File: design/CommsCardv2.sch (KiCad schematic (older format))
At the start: 0 parts

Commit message: Remove annotation
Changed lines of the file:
@@
 $EndSheet
 $Sheet
-S 2050 4150 1350 900
+S 2050 4100 1300 1450
 U 5A78E64E
 F0 "FlightComputer1" 50
 F1 "Input.sch" 50
+F2 "USB_DM" B L 2050 4850 50
+F3 "USB_DP" B L 2050 4950 50
+F4 "LOS_CLK" O R 3350 4200 50
+F5 "LOS_DATA" O R 3350 4300 50
+F6 "HIGHRATE_TX" O R 3350 4450 50
+F7 "HIGHRATE_RX" O R 3350 4550 50
+F8 "COMM2_TX" O R 3350 4700 50
+F9 "COMM2_RX" O R 3350 4800 50
+F10 "COMM1_TX" O R 3350 4950 50
+F11 "COMM1_RX" O R 3350 5050 50
+F12 "~PWREN" O R 3350 5200 50
+F13 "IN_CHARGE" I R 3350 5450 50
+F14 "WD_TICKLE" O R 3350 5300 50
 $EndSheet
 $Sheet
-S 2100 5500 1300 750
+S 2050 6350 1300 750
 U 5A78E661
 F0 "FlightComputer2" 50

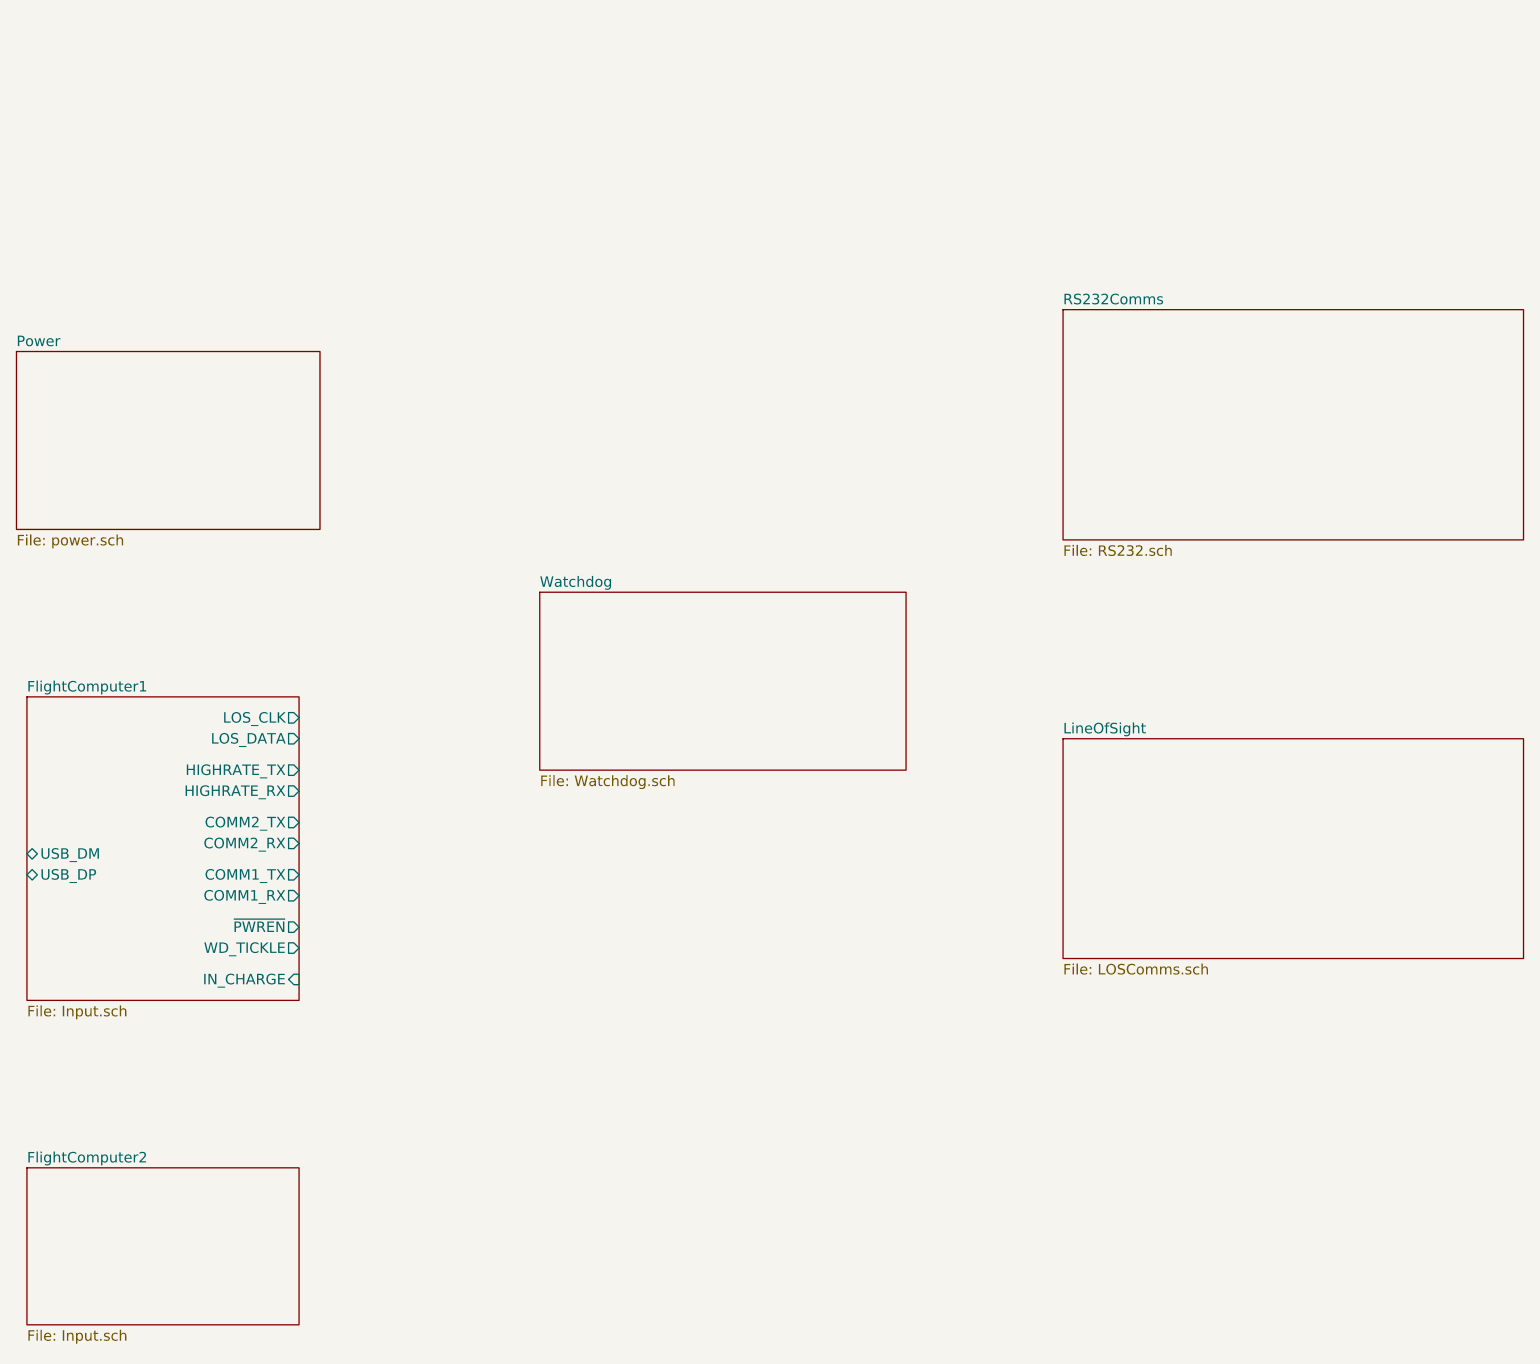
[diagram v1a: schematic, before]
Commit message: Connecting LOS inside FC connection
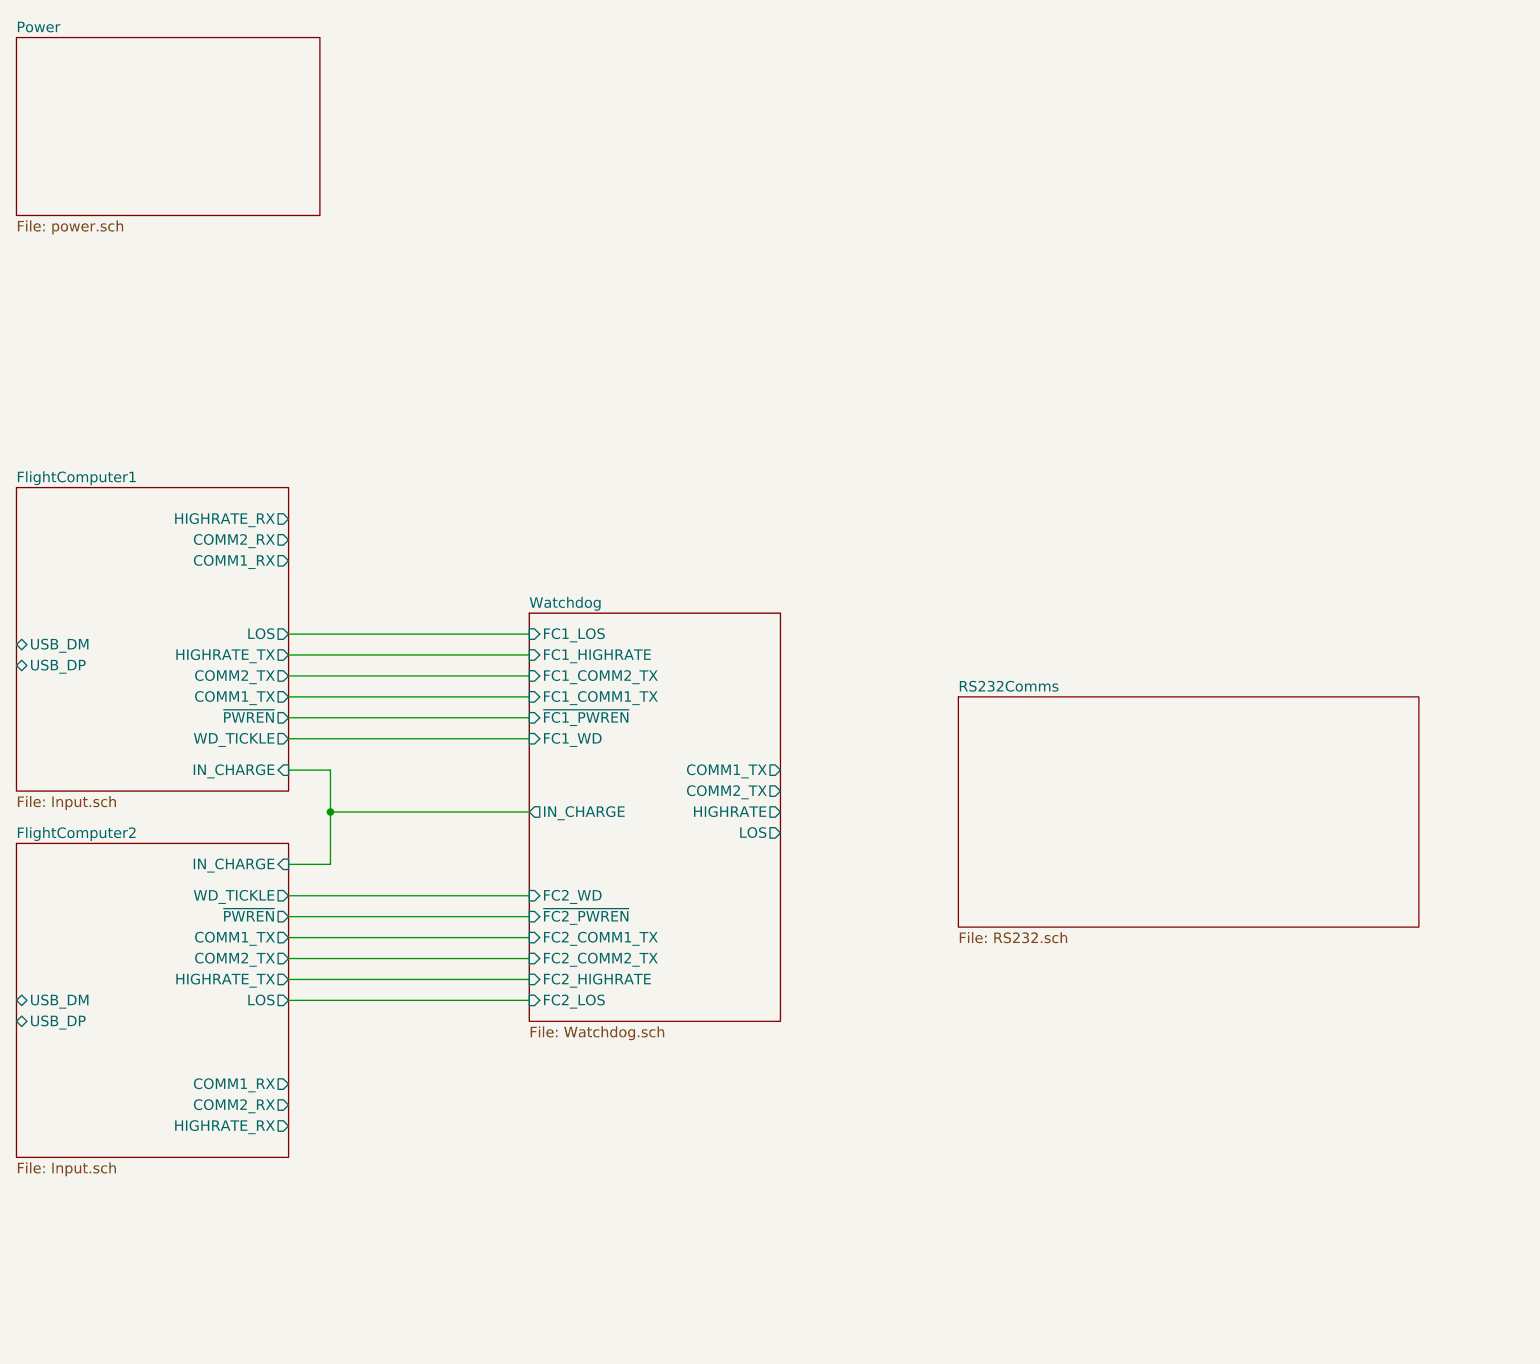
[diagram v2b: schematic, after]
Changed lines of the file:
@@
 $Descr A4 11693 8268
 encoding utf-8
-Sheet 1 7
+Sheet 1 8
 Title ""
 Date ""
@@
 $EndDescr
 $Sheet
-S 2000 2450 1450 850
+S 2000 950  1450 850
 U 5A78E52F
 F0 "Power" 50
@@
 $EndSheet
 $Sheet
-S 7000 4300 2200 1050
-U 5A78E5CC
-F0 "LineOfSight" 50
-F1 "LOSComms.sch" 50
-$EndSheet
-$Sheet
-S 7000 2250 2200 1100
+S 6500 4100 2200 1100
 U 5A78E5DD
 F0 "RS232Comms" 50
@@
 $EndSheet
 $Sheet
-S 4500 3600 1750 850
+S 4450 3700 1200 1950
 U 5A78E618
 F0 "Watchdog" 50
 F1 "Watchdog.sch" 50
+F2 "FC1_WD" I L 4450 4300 50
+F3 "FC2_WD" I L 4450 5050 50
+F4 "~FC2_PWREN" I L 4450 5150 50
+F5 "~FC1_PWREN" I L 4450 4200 50
+F6 "FC1_COMM1_TX" I L 4450 4100 50
+F7 "FC2_COMM1_TX" I L 4450 5250 50
+F8 "FC2_COMM2_TX" I L 4450 5350 50
+F9 "FC1_COMM2_TX" I L 4450 4000 50
+F10 "FC1_HIGHRATE" I L 4450 3900 50
+F11 "FC2_HIGHRATE" I L 4450 5450 50
+F12 "FC1_LOS" I L 4450 3800 50
+F13 "FC2_LOS" I L 4450 5550 50
+F14 "COMM1_TX" O R 5650 4450 50
+F15 "COMM2_TX" O R 5650 4550 50
+F16 "HIGHRATE" O R 5650 4650 50
+F17 "LOS" O R 5650 4750 50
+F18 "IN_CHARGE" O L 4450 4650 50
 $EndSheet
 $Sheet
-S 2050 4100 1300 1450
+S 2000 3100 1300 1450
 U 5A78E64E
 F0 "FlightComputer1" 50
 F1 "Input.sch" 50
-F2 "USB_DM" B L 2050 4850 50
-F3 "USB_DP" B L 2050 4950 50
-F4 "LOS_CLK" O R 3350 4200 50
-F5 "LOS_DATA" O R 3350 4300 50
-F6 "HIGHRATE_TX" O R 3350 4450 50
-F7 "HIGHRATE_RX" O R 3350 4550 50
-F8 "COMM2_TX" O R 3350 4700 50
-F9 "COMM2_RX" O R 3350 4800 50
-F10 "COMM1_TX" O R 3350 4950 50
-F11 "COMM1_RX" O R 3350 5050 50
-F12 "~PWREN" O R 3350 5200 50
-F13 "IN_CHARGE" I R 3350 5450 50
-F14 "WD_TICKLE" O R 3350 5300 50
+F2 "USB_DM" B L 2000 3850 50
+F3 "USB_DP" B L 2000 3950 50
+F4 "HIGHRATE_TX" O R 3300 3900 50
+F5 "HIGHRATE_RX" O R 3300 3250 50
+F6 "COMM2_TX" O R 3300 4000 50
+F7 "COMM2_RX" O R 3300 3350 50
+F8 "COMM1_TX" O R 3300 4100 50
+F9 "COMM1_RX" O R 3300 3450 50
+F10 "~PWREN" O R 3300 4200 50
+F11 "IN_CHARGE" I R 3300 4450 50
+F12 "WD_TICKLE" O R 3300 4300 50
+F13 "LOS" O R 3300 3800 50
 $EndSheet
 $Sheet
-S 2050 6350 1300 750
+S 2000 4800 1300 1500
 U 5A78E661
 F0 "FlightComputer2" 50
 F1 "Input.sch" 50
+F2 "USB_DM" B L 2000 5550 50
+F3 "USB_DP" B L 2000 5650 50
+F4 "HIGHRATE_TX" O R 3300 5450 50
+F5 "HIGHRATE_RX" O R 3300 6150 50
+F6 "COMM2_TX" O R 3300 5350 50
+F7 "COMM2_RX" O R 3300 6050 50
+F8 "COMM1_TX" O R 3300 5250 50
+F9 "COMM1_RX" O R 3300 5950 50
+F10 "~PWREN" O R 3300 5150 50
+F11 "IN_CHARGE" I R 3300 4900 50
+F12 "WD_TICKLE" O R 3300 5050 50
+F13 "LOS" O R 3300 5550 50
 $EndSheet
+Wire Wire Line
+	4450 4650 3500 4650
+Wire Wire Line
+	3500 4650 3500 4450
+Wire Wire Line
+	3500 4450 3300 4450
+Wire Wire Line
+	3300 4900 3500 4900
+Wire Wire Line
+	3500 4900 3500 4650
+Connection ~ 3500 4650
+Wire Wire Line
+	3300 4300 4450 4300
+Wire Wire Line
+	3300 4200 4450 4200
+Wire Wire Line
+	3300 4100 4450 4100
+Wire Wire Line
+	4450 4000 3300 4000
+Wire Wire Line
+	3300 3900 4450 3900
+Wire Wire Line
+	4450 3800 3300 3800
+Wire Wire Line
+	3300 5050 4450 5050
+Wire Wire Line
+	4450 5150 3300 5150
+Wire Wire Line
+	3300 5250 4450 5250
+Wire Wire Line
+	4450 5350 3300 5350
+Wire Wire Line
+	3300 5450 4450 5450
+Wire Wire Line
+	4450 5550 3300 5550
 $EndSCHEMATC

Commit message: Adding RS-232 Ports
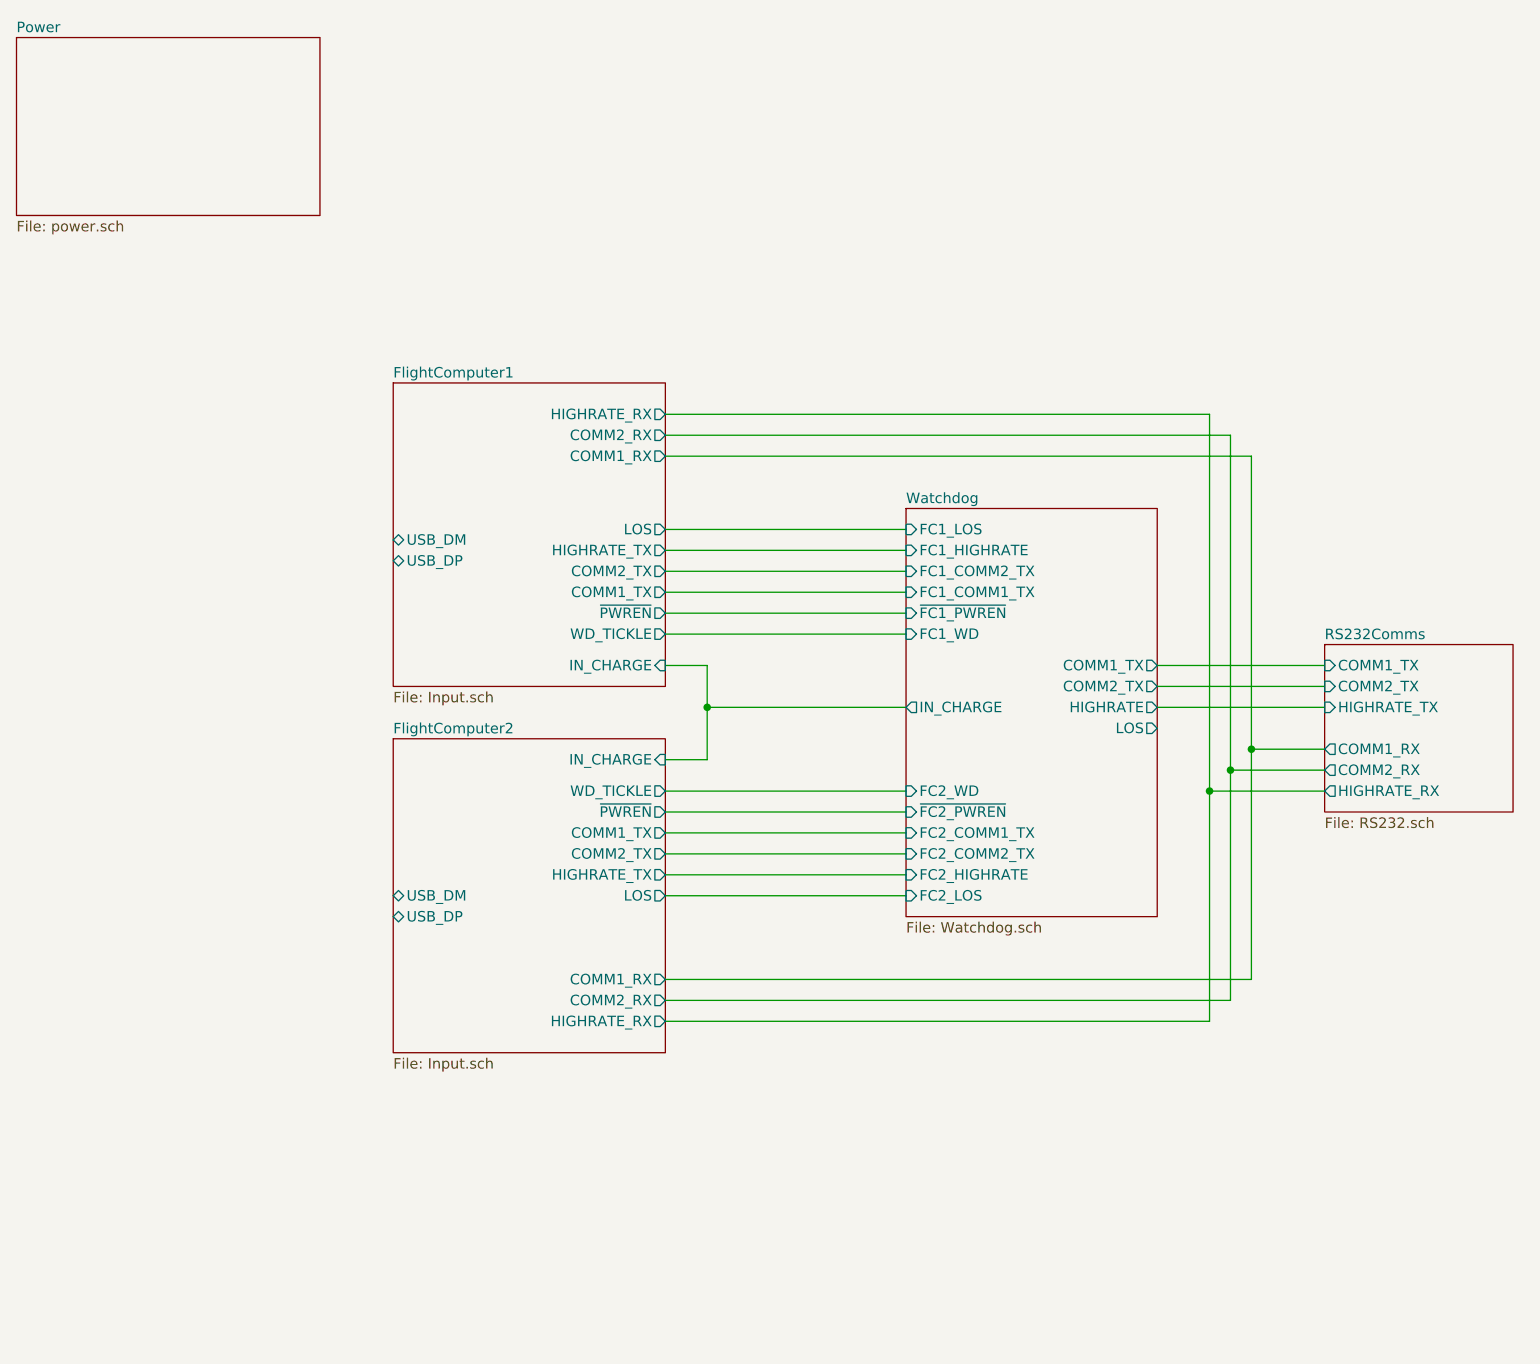
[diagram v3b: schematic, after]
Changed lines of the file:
@@
 $EndSheet
 $Sheet
-S 6500 4100 2200 1100
+S 8250 3850 900  800
 U 5A78E5DD
 F0 "RS232Comms" 50
 F1 "RS232.sch" 50
+F2 "COMM1_TX" I L 8250 3950 50
+F3 "COMM2_TX" I L 8250 4050 50
+F4 "HIGHRATE_TX" I L 8250 4150 50
+F5 "COMM1_RX" O L 8250 4350 50
+F6 "COMM2_RX" O L 8250 4450 50
+F7 "HIGHRATE_RX" O L 8250 4550 50
 $EndSheet
 $Sheet
-S 4450 3700 1200 1950
+S 6250 3200 1200 1950
 U 5A78E618
 F0 "Watchdog" 50
 F1 "Watchdog.sch" 50
-F2 "FC1_WD" I L 4450 4300 50
-F3 "FC2_WD" I L 4450 5050 50
-F4 "~FC2_PWREN" I L 4450 5150 50
-F5 "~FC1_PWREN" I L 4450 4200 50
-F6 "FC1_COMM1_TX" I L 4450 4100 50
-F7 "FC2_COMM1_TX" I L 4450 5250 50
-F8 "FC2_COMM2_TX" I L 4450 5350 50
-F9 "FC1_COMM2_TX" I L 4450 4000 50
-F10 "FC1_HIGHRATE" I L 4450 3900 50
-F11 "FC2_HIGHRATE" I L 4450 5450 50
-F12 "FC1_LOS" I L 4450 3800 50
-F13 "FC2_LOS" I L 4450 5550 50
-F14 "COMM1_TX" O R 5650 4450 50
-F15 "COMM2_TX" O R 5650 4550 50
-F16 "HIGHRATE" O R 5650 4650 50
-F17 "LOS" O R 5650 4750 50
-F18 "IN_CHARGE" O L 4450 4650 50
+F2 "FC1_WD" I L 6250 3800 50
+F3 "FC2_WD" I L 6250 4550 50
+F4 "~FC2_PWREN" I L 6250 4650 50
+F5 "~FC1_PWREN" I L 6250 3700 50
+F6 "FC1_COMM1_TX" I L 6250 3600 50
+F7 "FC2_COMM1_TX" I L 6250 4750 50
+F8 "FC2_COMM2_TX" I L 6250 4850 50
+F9 "FC1_COMM2_TX" I L 6250 3500 50
+F10 "FC1_HIGHRATE" I L 6250 3400 50
+F11 "FC2_HIGHRATE" I L 6250 4950 50
+F12 "FC1_LOS" I L 6250 3300 50
+F13 "FC2_LOS" I L 6250 5050 50
+F14 "COMM1_TX" O R 7450 3950 50
+F15 "COMM2_TX" O R 7450 4050 50
+F16 "HIGHRATE" O R 7450 4150 50
+F17 "LOS" O R 7450 4250 50
+F18 "IN_CHARGE" O L 6250 4150 50
 $EndSheet
 $Sheet
-S 2000 3100 1300 1450
+S 3800 2600 1300 1450
 U 5A78E64E
 F0 "FlightComputer1" 50
 F1 "Input.sch" 50
-F2 "USB_DM" B L 2000 3850 50
-F3 "USB_DP" B L 2000 3950 50
-F4 "HIGHRATE_TX" O R 3300 3900 50
-F5 "HIGHRATE_RX" O R 3300 3250 50
-F6 "COMM2_TX" O R 3300 4000 50
-F7 "COMM2_RX" O R 3300 3350 50
-F8 "COMM1_TX" O R 3300 4100 50
-F9 "COMM1_RX" O R 3300 3450 50
-F10 "~PWREN" O R 3300 4200 50
-F11 "IN_CHARGE" I R 3300 4450 50
-F12 "WD_TICKLE" O R 3300 4300 50
-F13 "LOS" O R 3300 3800 50
+F2 "USB_DM" B L 3800 3350 50
+F3 "USB_DP" B L 3800 3450 50
+F4 "HIGHRATE_TX" O R 5100 3400 50
+F5 "HIGHRATE_RX" O R 5100 2750 50
+F6 "COMM2_TX" O R 5100 3500 50
+F7 "COMM2_RX" O R 5100 2850 50
+F8 "COMM1_TX" O R 5100 3600 50
+F9 "COMM1_RX" O R 5100 2950 50
+F10 "~PWREN" O R 5100 3700 50
+F11 "IN_CHARGE" I R 5100 3950 50
+F12 "WD_TICKLE" O R 5100 3800 50
+F13 "LOS" O R 5100 3300 50
 $EndSheet
 $Sheet
-S 2000 4800 1300 1500
+S 3800 4300 1300 1500
 U 5A78E661
 F0 "FlightComputer2" 50
 F1 "Input.sch" 50
-F2 "USB_DM" B L 2000 5550 50
-F3 "USB_DP" B L 2000 5650 50
-F4 "HIGHRATE_TX" O R 3300 5450 50
-F5 "HIGHRATE_RX" O R 3300 6150 50
-F6 "COMM2_TX" O R 3300 5350 50
-F7 "COMM2_RX" O R 3300 6050 50
-F8 "COMM1_TX" O R 3300 5250 50
-F9 "COMM1_RX" O R 3300 5950 50
-F10 "~PWREN" O R 3300 5150 50
-F11 "IN_CHARGE" I R 3300 4900 50
-F12 "WD_TICKLE" O R 3300 5050 50
-F13 "LOS" O R 3300 5550 50
+F2 "USB_DM" B L 3800 5050 50
+F3 "USB_DP" B L 3800 5150 50
+F4 "HIGHRATE_TX" O R 5100 4950 50
+F5 "HIGHRATE_RX" O R 5100 5650 50
+F6 "COMM2_TX" O R 5100 4850 50
+F7 "COMM2_RX" O R 5100 5550 50
+F8 "COMM1_TX" O R 5100 4750 50
+F9 "COMM1_RX" O R 5100 5450 50
+F10 "~PWREN" O R 5100 4650 50
+F11 "IN_CHARGE" I R 5100 4400 50
+F12 "WD_TICKLE" O R 5100 4550 50
+F13 "LOS" O R 5100 5050 50
 $EndSheet
 Wire Wire Line
-	4450 4650 3500 4650
+	6250 4150 5300 4150
 Wire Wire Line
-	3500 4650 3500 4450
+	5300 4150 5300 3950
 Wire Wire Line
-	3500 4450 3300 4450
+	5300 3950 5100 3950
 Wire Wire Line
-	3300 4900 3500 4900
+	5100 4400 5300 4400
 Wire Wire Line
-	3500 4900 3500 4650
-Connection ~ 3500 4650
+	5300 4400 5300 4150
+Connection ~ 5300 4150
 Wire Wire Line
-	3300 4300 4450 4300
+	5100 3800 6250 3800
 Wire Wire Line
-	3300 4200 4450 4200
+	5100 3700 6250 3700
 Wire Wire Line
-	3300 4100 4450 4100
+	5100 3600 6250 3600
 Wire Wire Line
-	4450 4000 3300 4000
+	6250 3500 5100 3500
 Wire Wire Line
-	3300 3900 4450 3900
+	5100 3400 6250 3400
 Wire Wire Line
-	4450 3800 3300 3800
+	6250 3300 5100 3300
 Wire Wire Line
-	3300 5050 4450 5050
+	5100 4550 6250 4550
 Wire Wire Line
-	4450 5150 3300 5150
+	6250 4650 5100 4650
 Wire Wire Line
-	3300 5250 4450 5250
+	5100 4750 6250 4750
 Wire Wire Line
-	4450 5350 3300 5350
+	6250 4850 5100 4850
 Wire Wire Line
-	3300 5450 4450 5450
+	5100 4950 6250 4950
 Wire Wire Line
-	4450 5550 3300 5550
+	6250 5050 5100 5050
+Wire Wire Line
+	8250 4150 7450 4150
+Wire Wire Line
+	8250 4050 7450 4050
+Wire Wire Line
+	8250 3950 7450 3950
+Wire Wire Line
+	5100 5550 7800 5550
+Wire Wire Line
+	8250 4350 7900 4350
+Wire Wire Line
+	7900 4350 7900 2950
+Wire Wire Line
+	7900 2950 5100 2950
+Wire Wire Line
+	8250 4450 7800 4450
+Wire Wire Line
+	7800 4450 7800 2850
+Wire Wire Line
+	7800 2850 5100 2850
+Wire Wire Line
+	8250 4550 7700 4550
+Wire Wire Line
+	7700 4550 7700 2750
+Wire Wire Line
+	7700 4550 7700 5650
+Connection ~ 7700 4550
+Wire Wire Line
+	7700 5650 5100 5650
+Wire Wire Line
+	7800 4450 7800 5550
+Connection ~ 7800 4450
+Wire Wire Line
+	7900 4350 7900 5450
+Wire Wire Line
+	5100 5450 7900 5450
+Connection ~ 7900 4350
+Wire Wire Line
+	5100 2750 7700 2750
 $EndSCHEMATC
